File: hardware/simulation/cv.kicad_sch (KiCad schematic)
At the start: 22 parts, among them U1 ${SIM.PARAMS}, U2 ${SIM.PARAMS}, U3 ${SIM.PARAMS}

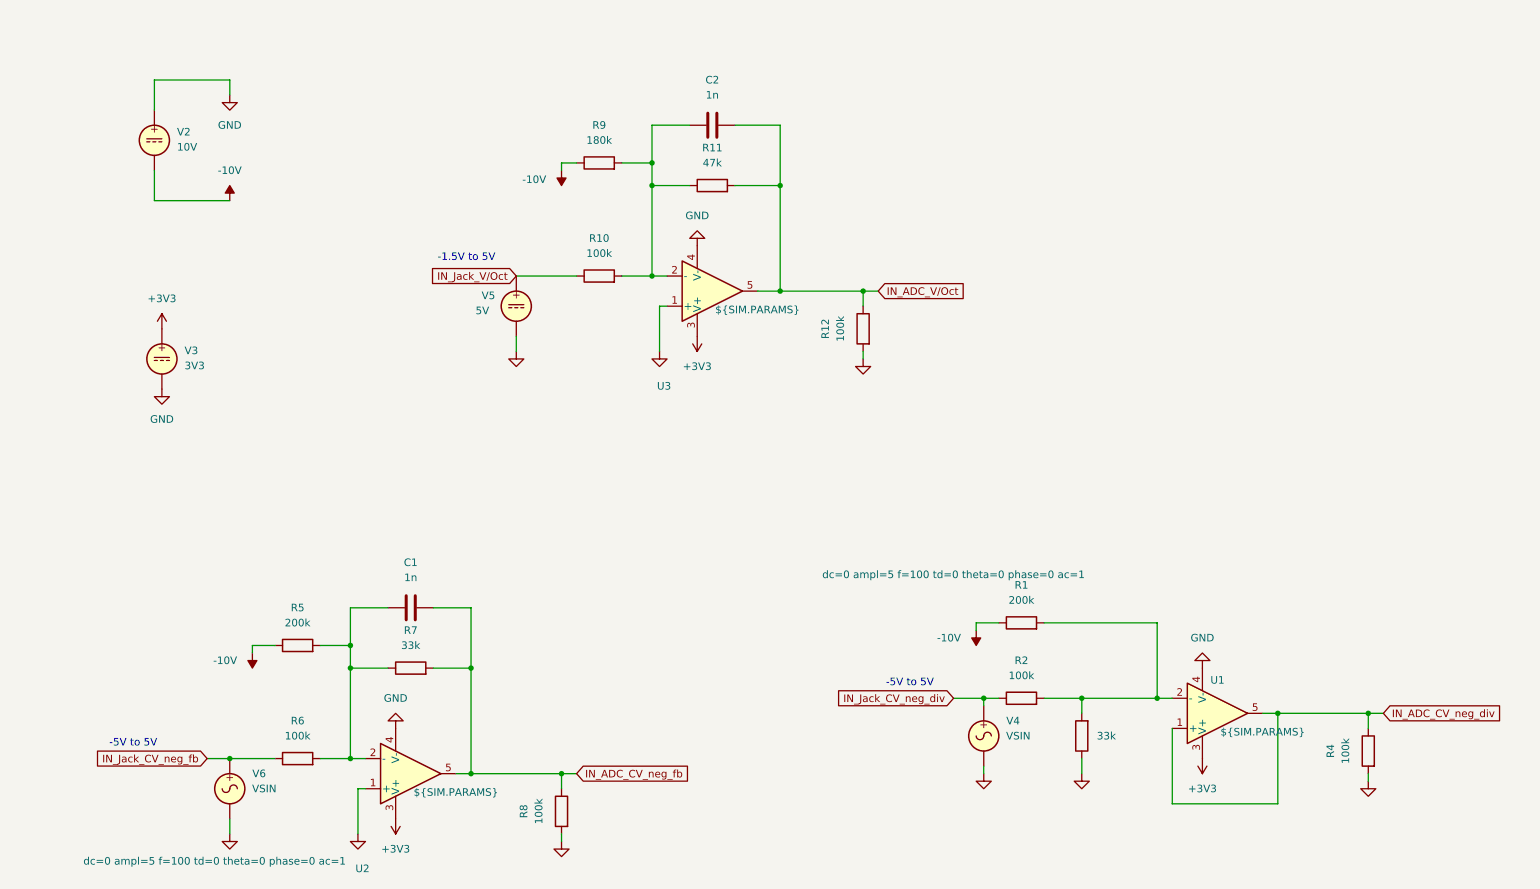
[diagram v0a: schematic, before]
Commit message: hw: simulation updates
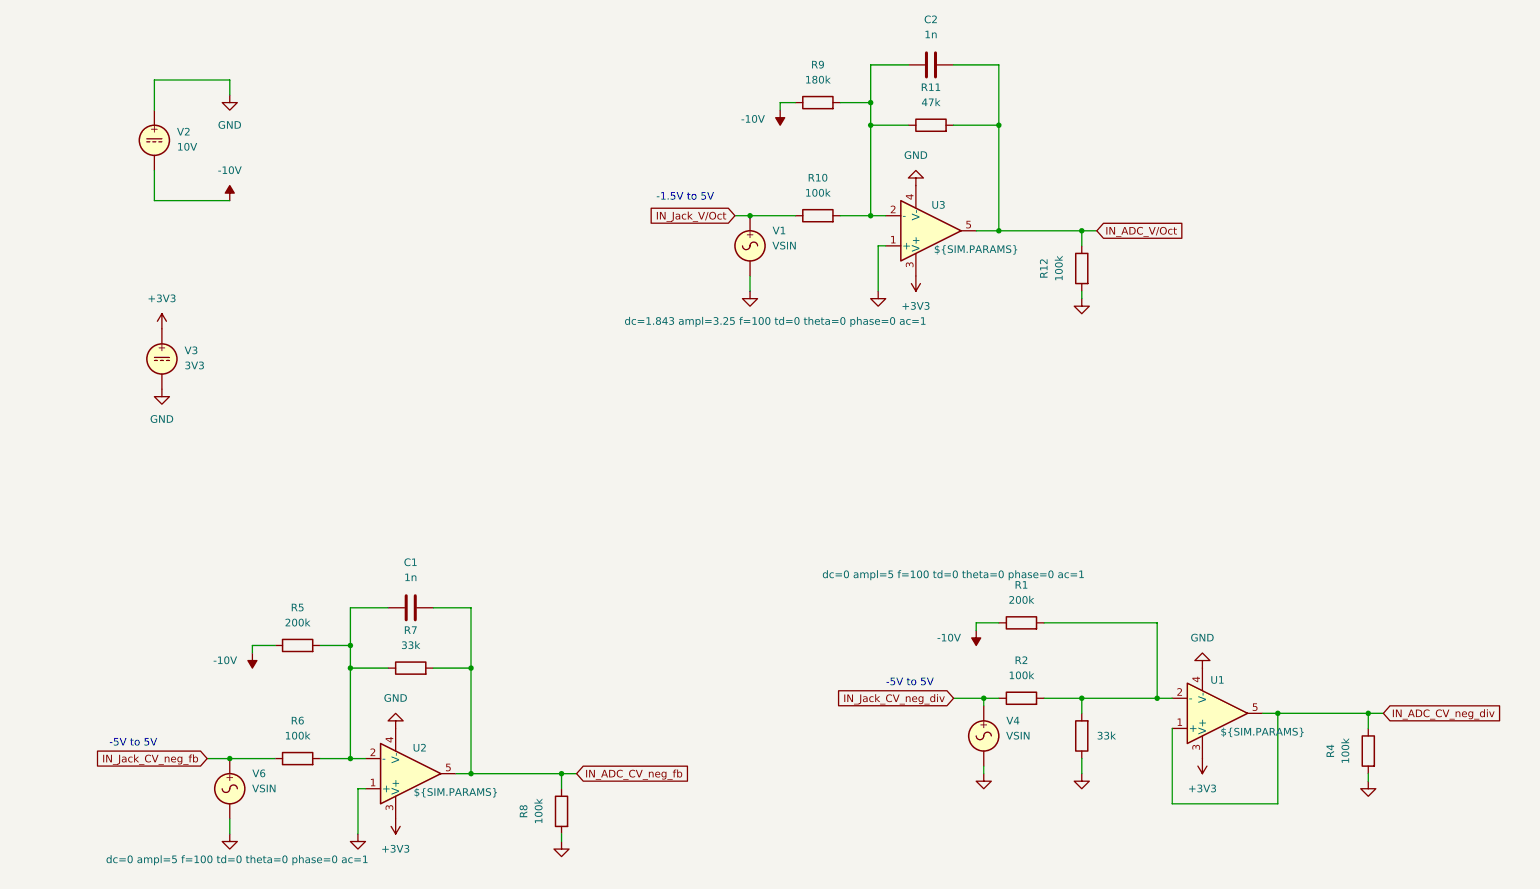
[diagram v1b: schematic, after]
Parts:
- removed V5: 5V, symbol Simulation_SPICE:VDC
- added V1: VSIN, symbol Simulation_SPICE:VSIN
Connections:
- net GND: now also V1.2
- net IN_Jack_V/Oct: now also V1.1
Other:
- moved on the sheet: C2, R10, R11, R12, R9, U3
